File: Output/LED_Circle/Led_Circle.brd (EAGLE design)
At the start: 20 x 13 mm, 22 parts

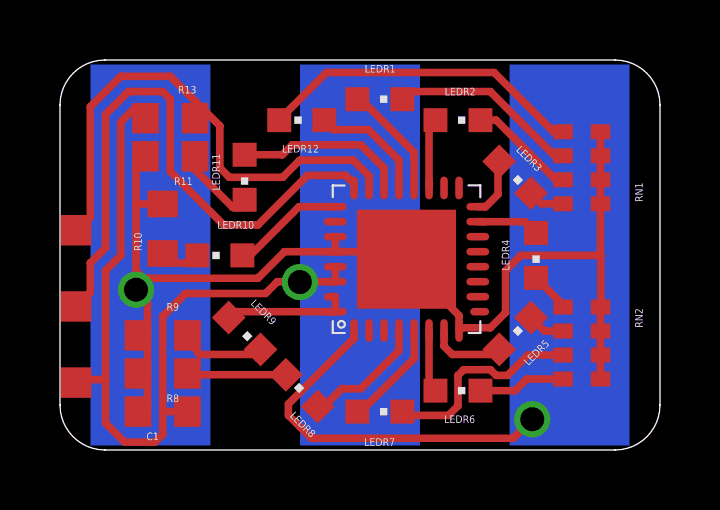
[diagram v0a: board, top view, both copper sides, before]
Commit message: Update Pinheader
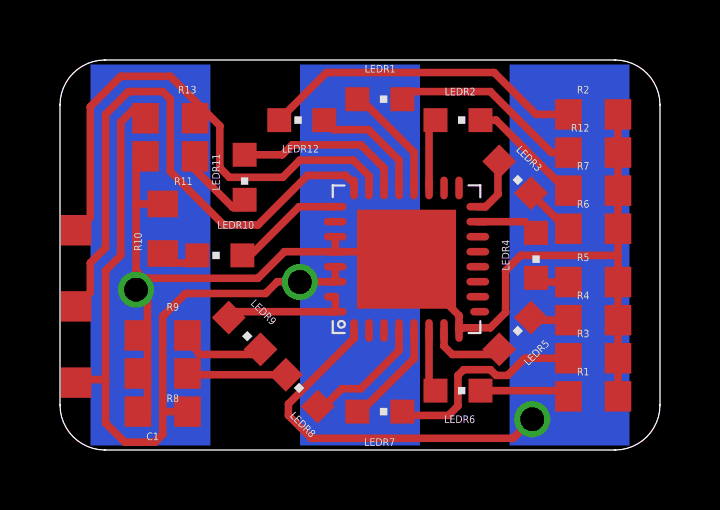
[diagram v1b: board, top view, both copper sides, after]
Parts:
- removed RN1, RN2: 68, resistor-dil:0603-ARC
- added R1, R12, R2, R3, R4, R5, R6, R7: 68, thar:603
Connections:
- net GND: now also R1.2, R12.2, R2.2, R3.2, R4.2, R5.2, R6.2, R7.2; no longer RN1.1, RN1.2, RN1.3, RN1.4, RN2.1, RN2.2, RN2.3, RN2.4
- net N$12: now also R1.1; no longer RN2.8
- net N$14: now also R4.1; no longer RN2.6
- net N$15: now also R5.1; no longer RN2.5
- net N$16: now also R6.1; no longer RN1.8
- net N$17: now also R7.1; no longer RN1.7
- net N$18: now also R12.1; no longer RN1.6
- net N$2: now also R3.1; no longer RN2.7
- net N$4: now also R2.1; no longer RN1.5
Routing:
- net GND: track 42.5 -> 44.1 mm
- net N$16: track 1.21 -> 1.74 mm
